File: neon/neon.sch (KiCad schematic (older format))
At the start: 25 parts, among them J1 V3V3-VIO, J2 V3V3-GND, J3 V3V3-GND, J4 V3V3-GND, J5 VBUS-VCC, U2 A, U3 B, U4 C, U5 D, U6 74HC595

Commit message: Sniffer PCB - draft
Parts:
- added H1, H2, H3, H4: MountingHole, MountingHole:MountingHole_3.2mm_M3, symbol Mechanical:MountingHole
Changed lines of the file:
@@
-$EndComp
-$Comp
-L FTDI:V3V3-GND J2
-U 1 1 5F4F5A0D
-P 7900 5000
-F 0 "J2" V 8100 4850 50  0000 L CNN
-F 1 "V3V3-GND" H 7900 4800 50  0001 C CNN
-F 2 "Connector_PinHeader_2.54mm:PinHeader_1x02_P2.54mm_Vertical" H 7900 5000 50  0001 C CNN
-F 3 "~" H 7900 5000 50  0001 C CNN
-	1    7900 5000
-	-1   0    0    1
 $EndComp
 $Comp
@@
 Wire Wire Line
 	7800 2950 7800 3800
+$Comp
+L Mechanical:MountingHole H4
+U 1 1 5F687DE6
+P 11000 6250
+F 0 "H4" H 10800 6300 50  0000 L CNN
+F 1 "MountingHole" H 10400 6200 50  0000 L CNN
+F 2 "MountingHole:MountingHole_3.2mm_M3" H 11000 6250 50  0001 C CNN
+F 3 "~" H 11000 6250 50  0001 C CNN
+	1    11000 6250
+	1    0    0    -1
+$EndComp
+$Comp
+L Mechanical:MountingHole H3
+U 1 1 5F689368
+P 11000 6000
+F 0 "H3" H 10800 6050 50  0000 L CNN
+F 1 "MountingHole" H 10400 5950 50  0000 L CNN
+F 2 "MountingHole:MountingHole_3.2mm_M3" H 11000 6000 50  0001 C CNN
+F 3 "~" H 11000 6000 50  0001 C CNN
+	1    11000 6000
+	1    0    0    -1
+$EndComp
+$Comp
+L Mechanical:MountingHole H2
+U 1 1 5F6917E6
+P 11000 5750
+F 0 "H2" H 10800 5800 50  0000 L CNN
+F 1 "MountingHole" H 10400 5700 50  0000 L CNN
+F 2 "MountingHole:MountingHole_3.2mm_M3" H 11000 5750 50  0001 C CNN
+F 3 "~" H 11000 5750 50  0001 C CNN
+	1    11000 5750
+	1    0    0    -1
+$EndComp
+$Comp
+L Mechanical:MountingHole H1
+U 1 1 5F699B09
+P 11000 5500
+F 0 "H1" H 10800 5550 50  0000 L CNN
+F 1 "MountingHole" H 10400 5450 50  0000 L CNN
+F 2 "MountingHole:MountingHole_3.2mm_M3" H 11000 5500 50  0001 C CNN
+F 3 "~" H 11000 5500 50  0001 C CNN
+	1    11000 5500
+	1    0    0    -1
+$EndComp
+$Comp
+L FTDI:V3V3-GND J2
+U 1 1 5F4F5A0D
+P 7900 5000
+F 0 "J2" V 8100 4850 50  0000 L CNN
+F 1 "V3V3-GND" H 7900 4800 50  0001 C CNN
+F 2 "Connector_PinHeader_2.54mm:PinHeader_1x02_P2.54mm_Vertical" H 7900 5000 50  0001 C CNN
+F 3 "~" H 7900 5000 50  0001 C CNN
+	1    7900 5000
+	-1   0    0    1
+$EndComp
 $EndSCHEMATC

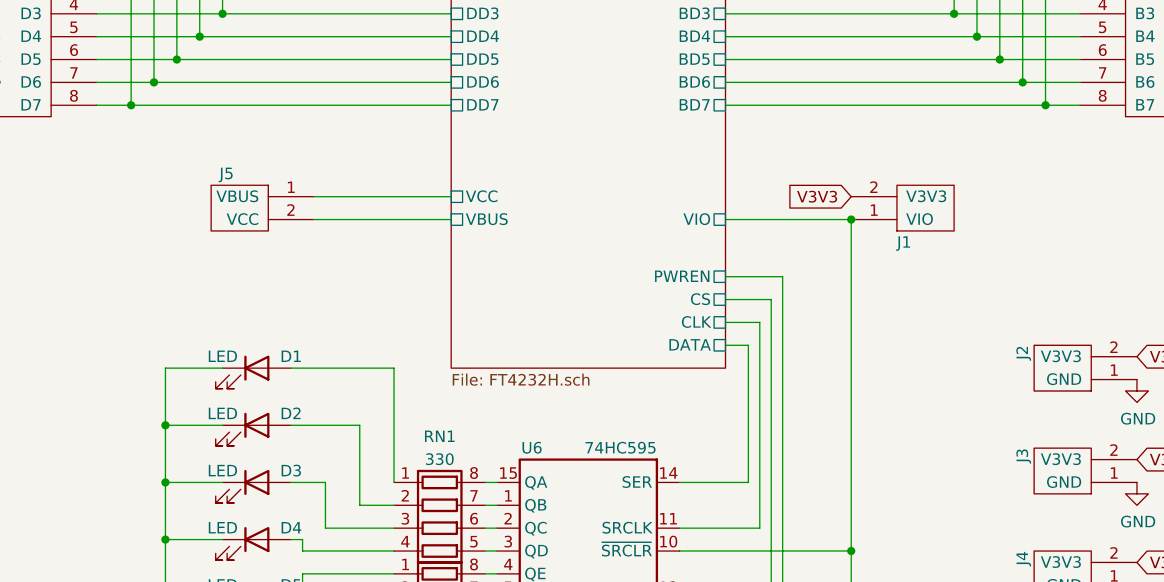
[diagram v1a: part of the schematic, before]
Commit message: All sniffers on PCB
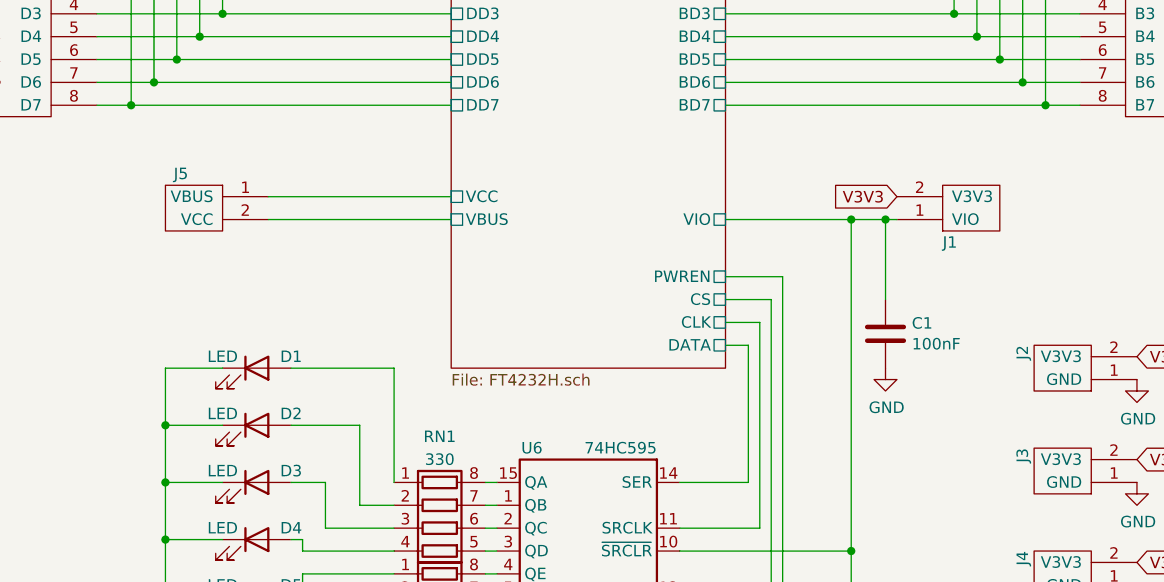
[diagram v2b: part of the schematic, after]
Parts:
- added C1: 100nF, Capacitor_SMD:C_0805_2012Metric, symbol Device:C
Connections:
- net FT4232H.sch/VIO: now also C1.1
- net GND: now also C1.2
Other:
- moved on the sheet: J1, J5
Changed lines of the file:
@@
 $EndDescr
 Wire Wire Line
-	4600 4300 5200 4300
+	4400 4300 5200 4300
 Wire Wire Line
 	5200 3400 4200 3400
@@
 Wire Wire Line
 	3650 3700 3900 3700
-Text GLabel 6950 4200 0    50   Input ~ 0
+Text GLabel 7150 4200 0    50   Input ~ 0
 V3V3
 Wire Wire Line
@@
 Wire Wire Line
 	6200 6050 6650 6050
-Connection ~ 6950 4300
 Wire Wire Line
 	6400 4300 6950 4300
@@
 	6950 4300 6950 5750
 Wire Wire Line
-	4600 4200 5200 4200
+	4400 4200 5200 4200
 Connection ~ 6650 6050
 Connection ~ 6950 6050
@@
 L FTDI:VBUS-VCC J5
 U 1 1 5F51B746
-P 4300 4200
-F 0 "J5" H 4350 4300 50  0000 L CNN
-F 1 "VBUS-VCC" H 4450 4000 50  0001 C CNN
-F 2 "Connector_PinHeader_2.54mm:PinHeader_1x02_P2.54mm_Vertical" H 4300 4200 50  0001 C CNN
-F 3 "~" H 4300 4200 50  0001 C CNN
-	1    4300 4200
+P 4100 4200
+F 0 "J5" H 4150 4300 50  0000 L CNN
+F 1 "VBUS-VCC" H 4250 4000 50  0001 C CNN
+F 2 "Connector_PinHeader_2.54mm:PinHeader_1x02_P2.54mm_Vertical" H 4100 4200 50  0001 C CNN
+F 3 "~" H 4100 4200 50  0001 C CNN
+	1    4100 4200
 	-1   0    0    -1
-$EndComp
-$Comp
-L FTDI:V3V3-VIO J1
-U 1 1 5F4B4881
-P 7250 4300
-F 0 "J1" H 7150 4400 50  0000 L CNN
-F 1 "V3V3-VIO" H 7250 4100 50  0001 C CNN
-F 2 "Connector_PinHeader_2.54mm:PinHeader_1x02_P2.54mm_Vertical" H 7250 4300 50  0001 C CNN
-F 3 "~" H 7250 4300 50  0001 C CNN
-	1    7250 4300
-	1    0    0    1
 $EndComp
 $Comp
@@
 	-1   0    0    1
 $EndComp
+$Comp
+L FTDI:V3V3-VIO J1
+U 1 1 5F4B4881
+P 7450 4300
+F 0 "J1" H 7350 4400 50  0000 L CNN
+F 1 "V3V3-VIO" H 7450 4100 50  0001 C CNN
+F 2 "Connector_PinHeader_2.54mm:PinHeader_1x02_P2.54mm_Vertical" H 7450 4300 50  0001 C CNN
+F 3 "~" H 7450 4300 50  0001 C CNN
+	1    7450 4300
+	1    0    0    1
+$EndComp
+Wire Wire Line
+	7150 4300 7100 4300
+Connection ~ 6950 4300
+Wire Wire Line
+	7100 4300 7100 4650
+Connection ~ 7100 4300
+Wire Wire Line
+	7100 4300 6950 4300
+$Comp
+L Device:C C1
+U 1 1 5F6FF541
+P 7100 4800
+F 0 "C1" H 7215 4846 50  0000 L CNN
+F 1 "100nF" H 7215 4755 50  0000 L CNN
+F 2 "Capacitor_SMD:C_0805_2012Metric" H 7138 4650 50  0001 C CNN
+F 3 "~" H 7100 4800 50  0001 C CNN
+	1    7100 4800
+	1    0    0    -1
+$EndComp
+$Comp
+L power:GND #PWR02
+U 1 1 5F6FFFFA
+P 7100 4950
+F 0 "#PWR02" H 7100 4700 50  0001 C CNN
+F 1 "GND" H 7105 4777 50  0000 C CNN
+F 2 "" H 7100 4950 50  0001 C CNN
+F 3 "" H 7100 4950 50  0001 C CNN
+	1    7100 4950
+	1    0    0    -1
+$EndComp
 $EndSCHEMATC

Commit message: Problems fixes
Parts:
- U2: renamed from U4; symbol FTDI:CBUS -> FTDI:C
- U3: symbol FTDI:BBUS -> FTDI:B
- U4: renamed from U2; symbol FTDI:ABUS -> FTDI:A
- U5: symbol FTDI:DBUS -> FTDI:D
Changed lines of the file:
@@
 $EndComp
 $Comp
-L FTDI:DBUS U5
+L FTDI:D U5
 U 1 1 5F52AE75
 P 3450 3400
@@
 $EndComp
 $Comp
-L FTDI:CBUS U4
+L FTDI:C U2
 U 1 1 5F520AE1
 P 3450 1850
-F 0 "U4" H 3950 1850 50  0000 R CNN
+F 0 "U2" H 3950 1850 50  0000 R CNN
 F 1 "C" H 3900 1750 50  0000 R CNN
 F 2 "neon_footprints:PinHeader_1x08_P2.54mm_Vertical" H 3425 2525 50  0001 C CNN
@@
 $EndComp
 $Comp
-L FTDI:BBUS U3
+L FTDI:B U3
 U 1 1 5F51EDE5
 P 8150 3400
@@
 $EndComp
 $Comp
-L FTDI:ABUS U2
+L FTDI:A U4
 U 1 1 5F56E993
 P 8150 1850
-F 0 "U2" H 8550 1850 50  0000 L CNN
+F 0 "U4" H 8550 1850 50  0000 L CNN
 F 1 "A" H 8550 1750 50  0000 L CNN
 F 2 "neon_footprints:PinHeader_1x08_P2.54mm_Vertical" H 8125 2525 50  0001 C CNN

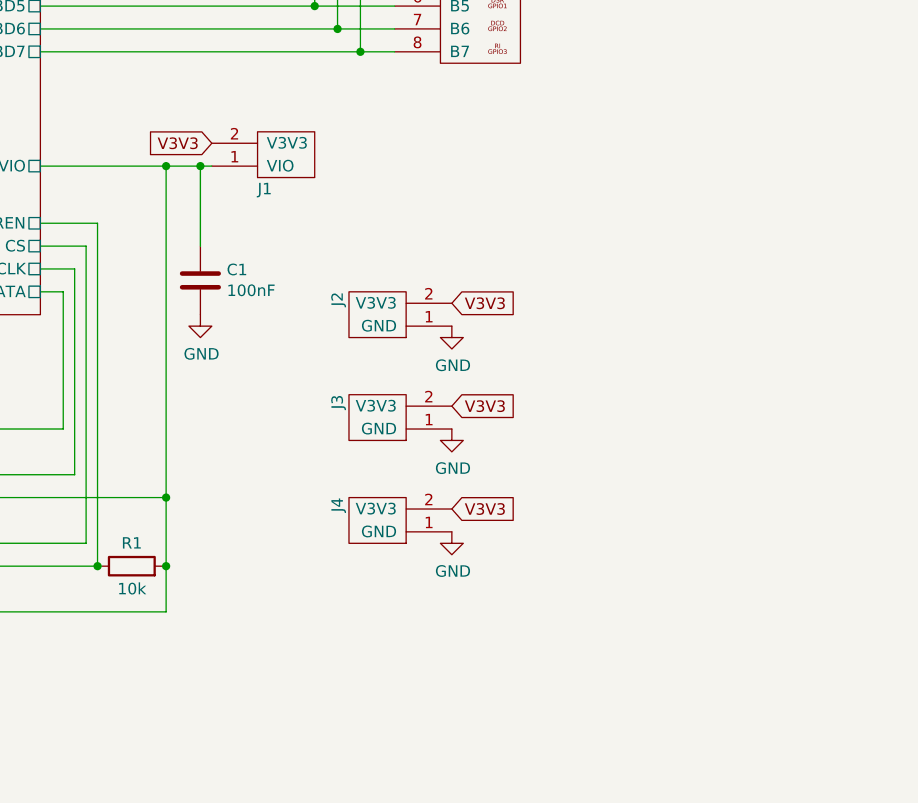
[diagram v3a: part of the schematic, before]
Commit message: Add 3x2 connector for GND&3v3
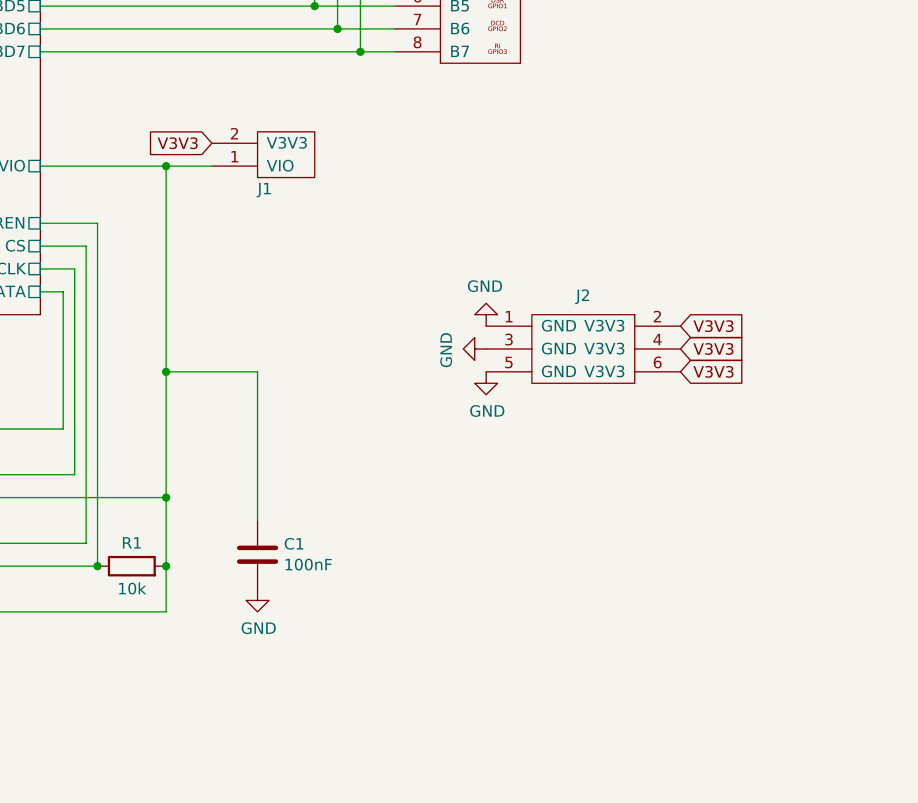
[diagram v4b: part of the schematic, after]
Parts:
- removed J2, J3, J4: V3V3-GND, Connector_PinHeader_2.54mm:PinHeader_1x02_P2.54mm_Vertical, symbol FTDI:V3V3-GND
- added J2: 3xV3V3-GND, Connector_PinHeader_2.54mm:PinHeader_2x03_P2.54mm_Vertical, symbol FTDI:3xV3V3-GND
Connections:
- net GND: now also J2.1 (GND), J2.3 (GND), J2.5 (GND)
- net V3V3: now also J2.2 (V3V3), J2.4 (V3V3), J2.6 (V3V3)
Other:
- moved on the sheet: C1
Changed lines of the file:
@@
 Wire Wire Line
 	6400 1750 7300 1750
-Text GLabel 8200 5350 2    50   Input ~ 0
-V3V3
-Text GLabel 8200 5800 2    50   Input ~ 0
-V3V3
-Text GLabel 8200 4900 2    50   Input ~ 0
-V3V3
 Wire Wire Line
 	6400 1650 7200 1650
@@
 	6400 4300 6950 4300
 Wire Wire Line
-	6950 4300 6950 5750
+	6950 4300 6950 5200
 Wire Wire Line
 	4400 4200 5200 4200
@@
 $EndComp
 $Comp
-L power:GND #PWR07
-U 1 1 5F4F5A13
-P 8200 5000
-F 0 "#PWR07" H 8200 4750 50  0001 C CNN
-F 1 "GND" H 8205 4827 50  0000 C CNN
-F 2 "" H 8200 5000 50  0001 C CNN
-F 3 "" H 8200 5000 50  0001 C CNN
-	1    8200 5000
-	1    0    0    -1
-$EndComp
-$Comp
-L power:GND #PWR06
-U 1 1 5F4F4975
-P 8200 5900
-F 0 "#PWR06" H 8200 5650 50  0001 C CNN
-F 1 "GND" H 8205 5727 50  0000 C CNN
-F 2 "" H 8200 5900 50  0001 C CNN
-F 3 "" H 8200 5900 50  0001 C CNN
-	1    8200 5900
-	1    0    0    -1
-$EndComp
-$Comp
-L FTDI:V3V3-GND J4
-U 1 1 5F4F496F
-P 7900 5900
-F 0 "J4" V 8100 5750 50  0000 L CNN
-F 1 "V3V3-GND" H 7900 5700 50  0001 C CNN
-F 2 "Connector_PinHeader_2.54mm:PinHeader_1x02_P2.54mm_Vertical" H 7900 5900 50  0001 C CNN
-F 3 "~" H 7900 5900 50  0001 C CNN
-	1    7900 5900
-	-1   0    0    1
-$EndComp
-$Comp
-L power:GND #PWR05
-U 1 1 5F4DA0BC
-P 8200 5450
-F 0 "#PWR05" H 8200 5200 50  0001 C CNN
-F 1 "GND" H 8205 5277 50  0000 C CNN
-F 2 "" H 8200 5450 50  0001 C CNN
-F 3 "" H 8200 5450 50  0001 C CNN
-	1    8200 5450
-	1    0    0    -1
-$EndComp
-$Comp
-L FTDI:V3V3-GND J3
-U 1 1 5F4D75A0
-P 7900 5450
-F 0 "J3" V 8100 5300 50  0000 L CNN
-F 1 "V3V3-GND" H 7900 5250 50  0001 C CNN
-F 2 "Connector_PinHeader_2.54mm:PinHeader_1x02_P2.54mm_Vertical" H 7900 5450 50  0001 C CNN
-F 3 "~" H 7900 5450 50  0001 C CNN
-	1    7900 5450
-	-1   0    0    1
-$EndComp
-$Comp
 L power:GND #PWR0102
 U 1 1 5F61BEF4
@@
 $EndComp
 $Comp
-L FTDI:V3V3-GND J2
-U 1 1 5F4F5A0D
-P 7900 5000
-F 0 "J2" V 8100 4850 50  0000 L CNN
-F 1 "V3V3-GND" H 7900 4800 50  0001 C CNN
-F 2 "Connector_PinHeader_2.54mm:PinHeader_1x02_P2.54mm_Vertical" H 7900 5000 50  0001 C CNN
-F 3 "~" H 7900 5000 50  0001 C CNN
-	1    7900 5000
-	-1   0    0    1
-$EndComp
-$Comp
 L FTDI:V3V3-VIO J1
 U 1 1 5F4B4881
@@
 	1    0    0    1
 $EndComp
-Wire Wire Line
-	7150 4300 7100 4300
 Connection ~ 6950 4300
-Wire Wire Line
-	7100 4300 7100 4650
-Connection ~ 7100 4300
-Wire Wire Line
-	7100 4300 6950 4300
+$Comp
+L power:GND #PWR02
+U 1 1 5F6FFFFA
+P 7350 6150
+F 0 "#PWR02" H 7350 5900 50  0001 C CNN
+F 1 "GND" H 7355 5977 50  0000 C CNN
+F 2 "" H 7350 6150 50  0001 C CNN
+F 3 "" H 7350 6150 50  0001 C CNN
+	1    7350 6150
+	1    0    0    -1
+$EndComp
+Wire Wire Line
+	6950 4300 7150 4300
 $Comp
 L Device:C C1
 U 1 1 5F6FF541
-P 7100 4800
-F 0 "C1" H 7215 4846 50  0000 L CNN
-F 1 "100nF" H 7215 4755 50  0000 L CNN
-F 2 "Capacitor_SMD:C_0805_2012Metric" H 7138 4650 50  0001 C CNN
-F 3 "~" H 7100 4800 50  0001 C CNN
-	1    7100 4800
-	1    0    0    -1
-$EndComp
-$Comp
-L power:GND #PWR02
-U 1 1 5F6FFFFA
-P 7100 4950
-F 0 "#PWR02" H 7100 4700 50  0001 C CNN
-F 1 "GND" H 7105 4777 50  0000 C CNN
-F 2 "" H 7100 4950 50  0001 C CNN
-F 3 "" H 7100 4950 50  0001 C CNN
-	1    7100 4950
-	1    0    0    -1
-$EndComp
+P 7350 6000
+F 0 "C1" H 7465 6046 50  0000 L CNN
+F 1 "100nF" H 7465 5955 50  0000 L CNN
+F 2 "Capacitor_SMD:C_0805_2012Metric" H 7388 5850 50  0001 C CNN
+F 3 "~" H 7350 6000 50  0001 C CNN
+	1    7350 6000
+	1    0    0    -1
+$EndComp
+Wire Wire Line
+	6950 5200 7350 5200
+Wire Wire Line
+	7350 5200 7350 5850
+Connection ~ 6950 5200
+Wire Wire Line
+	6950 5200 6950 5750
+$Comp
+L FTDI:3xV3V3-GND J2
+U 1 1 5F5754BA
+P 8650 5000
+F 0 "J2" H 8775 5133 50  0000 C CNN
+F 1 "3xV3V3-GND" H 8800 4700 50  0001 C CNN
+F 2 "Connector_PinHeader_2.54mm:PinHeader_2x03_P2.54mm_Vertical" H 8650 5000 50  0001 C CNN
+F 3 "~" H 8650 5000 50  0001 C CNN
+	1    8650 5000
+	1    0    0    -1
+$EndComp
+$Comp
+L power:GND #PWR05
+U 1 1 5F576283
+P 8350 5200
+F 0 "#PWR05" H 8350 4950 50  0001 C CNN
+F 1 "GND" H 8355 5027 50  0000 C CNN
+F 2 "" H 8350 5200 50  0001 C CNN
+F 3 "" H 8350 5200 50  0001 C CNN
+	1    8350 5200
+	1    0    0    -1
+$EndComp
+$Comp
+L power:GND #PWR03
+U 1 1 5F5907B8
+P 8350 5000
+F 0 "#PWR03" H 8350 4750 50  0001 C CNN
+F 1 "GND" H 8355 4827 50  0000 C CNN
+F 2 "" H 8350 5000 50  0001 C CNN
+F 3 "" H 8350 5000 50  0001 C CNN
+	1    8350 5000
+	-1   0    0    1
+$EndComp
+$Comp
+L power:GND #PWR04
+U 1 1 5F590D03
+P 8350 5100
+F 0 "#PWR04" H 8350 4850 50  0001 C CNN
+F 1 "GND" H 8355 4927 50  0000 C CNN
+F 2 "" H 8350 5100 50  0001 C CNN
+F 3 "" H 8350 5100 50  0001 C CNN
+	1    8350 5100
+	0    1    1    0
+$EndComp
+Text GLabel 9200 5000 2    50   Input ~ 0
+V3V3
+Text GLabel 9200 5100 2    50   Input ~ 0
+V3V3
+Text GLabel 9200 5200 2    50   Input ~ 0
+V3V3
 $EndSCHEMATC

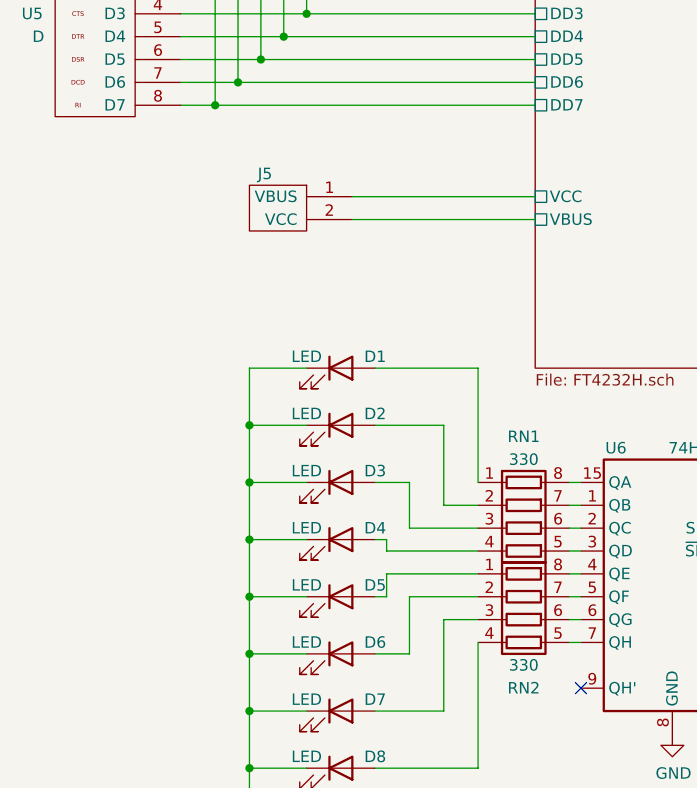
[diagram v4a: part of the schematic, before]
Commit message: Add LED to VBUS
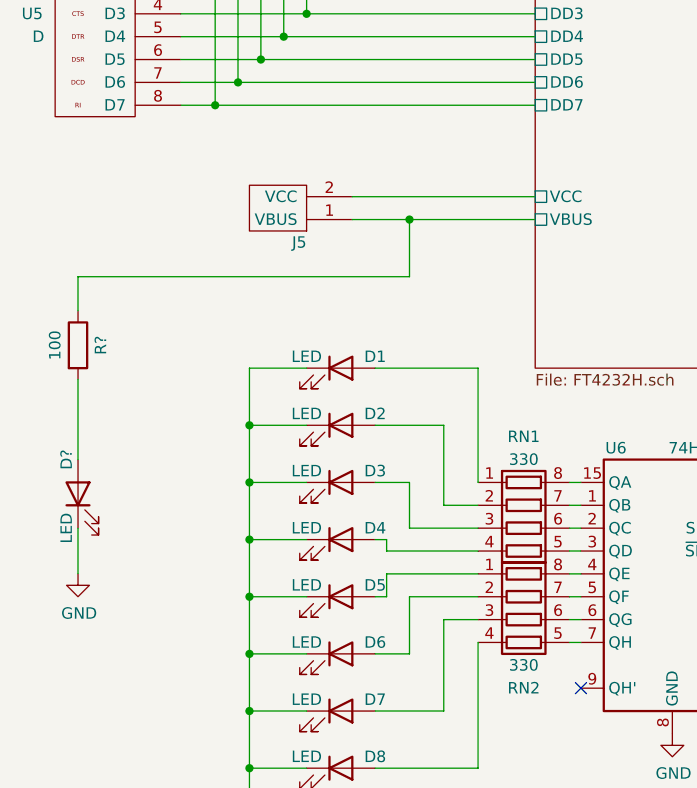
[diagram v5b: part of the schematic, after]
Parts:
- added D?: LED, neon_footprints:LED_0805_2012Metric, symbol Device:LED
- added R?: 100, Resistor_SMD:R_0805_2012Metric, symbol Device:R
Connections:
- net FT4232H.sch/VBUS: now also J5.1 (VBUS), R?.1; no longer J5.2 (VCC)
- net FT4232H.sch/VCC: now also J5.2 (VCC); no longer J5.1 (VBUS)
- net GND: now also D?.1 (K)
- new net: D?.2 (A), R?.2
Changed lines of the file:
@@
 $EndDescr
 Wire Wire Line
-	4400 4300 5200 4300
+	4400 4300 4650 4300
 Wire Wire Line
 	5200 3400 4200 3400
@@
 	4950 5750 4550 5750
 Wire Wire Line
-	4500 4950 4950 4950
-Wire Wire Line
 	4550 5750 4550 5700
 Wire Wire Line
@@
 Wire Wire Line
 	4650 5650 4950 5650
-Wire Wire Line
-	3950 4950 4200 4950
 Wire Wire Line
 	4200 5200 3950 5200
@@
 $EndComp
 $Comp
-L Device:LED D1
-U 1 1 5F56F686
-P 4350 4950
-F 0 "D1" H 4500 5000 50  0000 C CNN
-F 1 "LED" H 4200 5000 50  0000 C CNN
-F 2 "neon_footprints:LED_0805_2012Metric" H 4350 4950 50  0001 C CNN
-F 3 "~" H 4350 4950 50  0001 C CNN
-	1    4350 4950
-	1    0    0    -1
-$EndComp
-$Comp
 L FTDI:R_Pack04 RN2
 U 1 1 5F54B400
@@
 L FTDI:VBUS-VCC J5
 U 1 1 5F51B746
-P 4100 4200
-F 0 "J5" H 4150 4300 50  0000 L CNN
-F 1 "VBUS-VCC" H 4250 4000 50  0001 C CNN
-F 2 "Connector_PinHeader_2.54mm:PinHeader_1x02_P2.54mm_Vertical" H 4100 4200 50  0001 C CNN
-F 3 "~" H 4100 4200 50  0001 C CNN
-	1    4100 4200
-	-1   0    0    -1
+P 4100 4300
+F 0 "J5" H 4000 4400 50  0000 L CNN
+F 1 "VBUS-VCC" H 4250 4100 50  0001 C CNN
+F 2 "Connector_PinHeader_2.54mm:PinHeader_1x02_P2.54mm_Vertical" H 4100 4300 50  0001 C CNN
+F 3 "~" H 4100 4300 50  0001 C CNN
+	1    4100 4300
+	-1   0    0    1
 $EndComp
 $Comp
@@
 Text GLabel 9200 5200 2    50   Input ~ 0
 V3V3
+$Comp
+L Device:LED D1
+U 1 1 5F56F686
+P 4350 4950
+F 0 "D1" H 4500 5000 50  0000 C CNN
+F 1 "LED" H 4200 5000 50  0000 C CNN
+F 2 "neon_footprints:LED_0805_2012Metric" H 4350 4950 50  0001 C CNN
+F 3 "~" H 4350 4950 50  0001 C CNN
+	1    4350 4950
+	1    0    0    -1
+$EndComp
+Wire Wire Line
+	3950 4950 4200 4950
+Wire Wire Line
+	4500 4950 4950 4950
+Wire Wire Line
+	3200 4700 3200 4550
+Wire Wire Line
+	3200 4550 4650 4550
+Wire Wire Line
+	4650 4550 4650 4300
+Connection ~ 4650 4300
+Wire Wire Line
+	4650 4300 5200 4300
+$Comp
+L power:GND #PWR?
+U 1 1 5F529E27
+P 3200 5850
+F 0 "#PWR?" H 3200 5600 50  0001 C CNN
+F 1 "GND" H 3205 5677 50  0000 C CNN
+F 2 "" H 3200 5850 50  0001 C CNN
+F 3 "" H 3200 5850 50  0001 C CNN
+	1    3200 5850
+	1    0    0    -1
+$EndComp
+$Comp
+L Device:R R?
+U 1 1 5F53C653
+P 3200 4850
+F 0 "R?" V 3300 4850 50  0000 C CNN
+F 1 "100" V 3100 4850 50  0000 C CNN
+F 2 "Resistor_SMD:R_0805_2012Metric" V 3130 4850 50  0001 C CNN
+F 3 "~" H 3200 4850 50  0001 C CNN
+	1    3200 4850
+	1    0    0    -1
+$EndComp
+Wire Wire Line
+	3200 5650 3200 5850
+$Comp
+L Device:LED D?
+U 1 1 5F515BB1
+P 3200 5500
+F 0 "D?" H 3350 5550 50  0000 C CNN
+F 1 "LED" H 3050 5550 50  0000 C CNN
+F 2 "neon_footprints:LED_0805_2012Metric" H 3200 5500 50  0001 C CNN
+F 3 "~" H 3200 5500 50  0001 C CNN
+	1    3200 5500
+	0    -1   -1   0
+$EndComp
+Wire Wire Line
+	3200 5350 3200 5000
 $EndSCHEMATC

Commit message: Bigger letters & remove random dot
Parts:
- gave numbers to parts that had none: 2
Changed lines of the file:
@@
 	4650 4300 5200 4300
 $Comp
-L power:GND #PWR?
+L power:GND #PWR06
 U 1 1 5F529E27
 P 3200 5850
-F 0 "#PWR?" H 3200 5600 50  0001 C CNN
+F 0 "#PWR06" H 3200 5600 50  0001 C CNN
 F 1 "GND" H 3205 5677 50  0000 C CNN
 F 2 "" H 3200 5850 50  0001 C CNN
@@
 $EndComp
 $Comp
-L Device:R R?
+L Device:R R2
 U 1 1 5F53C653
 P 3200 4850
-F 0 "R?" V 3300 4850 50  0000 C CNN
+F 0 "R2" V 3300 4850 50  0000 C CNN
 F 1 "100" V 3100 4850 50  0000 C CNN
 F 2 "Resistor_SMD:R_0805_2012Metric" V 3130 4850 50  0001 C CNN
@@
 	3200 5650 3200 5850
 $Comp
-L Device:LED D?
+L Device:LED D9
 U 1 1 5F515BB1
 P 3200 5500
-F 0 "D?" H 3350 5550 50  0000 C CNN
+F 0 "D9" H 3350 5550 50  0000 C CNN
 F 1 "LED" H 3050 5550 50  0000 C CNN
 F 2 "neon_footprints:LED_0805_2012Metric" H 3200 5500 50  0001 C CNN
